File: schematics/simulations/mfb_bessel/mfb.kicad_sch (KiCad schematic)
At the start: 11 parts, among them U2 INA849D, U3 OPA182

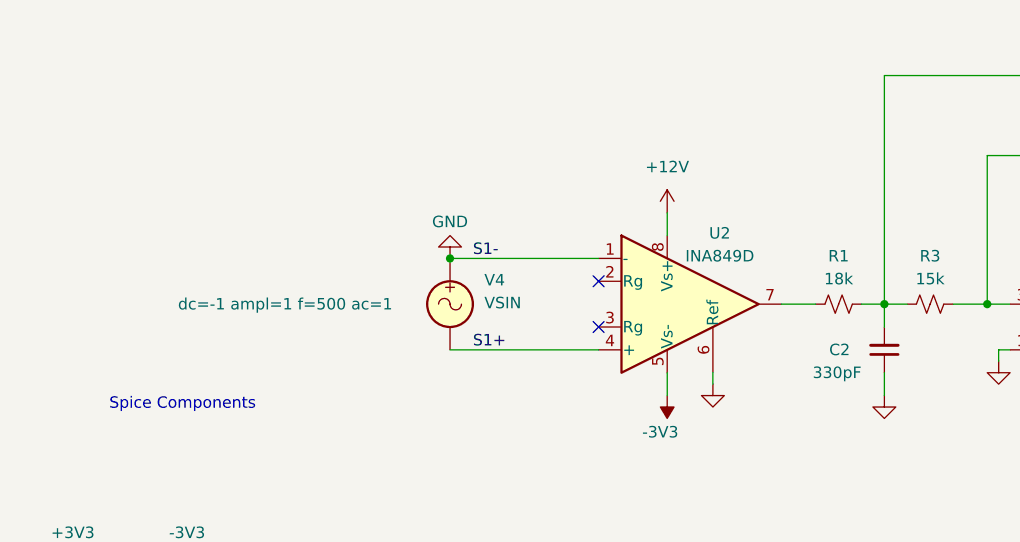
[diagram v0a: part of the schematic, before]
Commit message: feat(sim): swap for AD8422
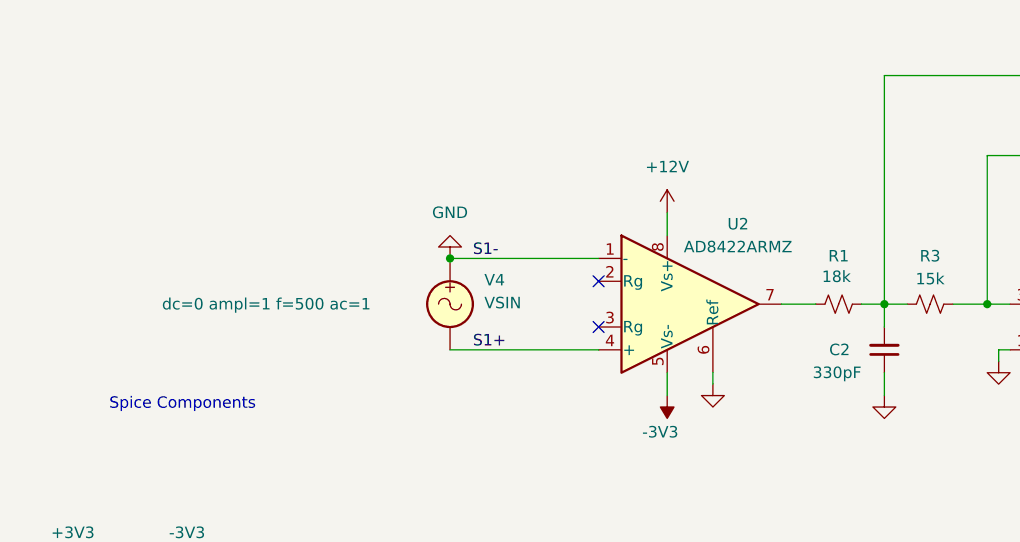
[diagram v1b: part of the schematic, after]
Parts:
- removed U2: INA849D, symbol Link-Components:INA849D
- added U2: AD8422ARMZ, symbol Amplifier_Instrumentation:AD8422ARMZ
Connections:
- net +12V: now also U2.8 (Vs+)
- net -3V3: now also U2.5 (Vs-)
- net 0: now also U2.1 (-), U2.6 (Ref)
- net S1+: now also U2.4 (+)
- net at R1.1: now also U2.7
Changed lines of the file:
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@@
+	)
+	(junction
+		(at 111.76 58.42)
+		(diameter 0)
+		(color 0 0 0 0)
 	)
 	(junction
 		(at 82.55 109.22)
-		(diameter 0)
-		(color 0 0 0 0)
-	)
-	(junction
-		(at 111.76 58.42)
 		(diameter 0)
 		(color 0 0 0 0)
@@
 			)
 		)
-		(property "Sim.Params" "dc=-1 ampl=1 f=500 ac=1"
-			(at 81.534 63.5 0)
+		(property "Sim.Params" "dc=0 ampl=1 f=500 ac=1"
+			(at 79.756 63.5 0)
 			(show_name no)
 			(do_not_autoplace no)
@@
 				(path "/404b3b71-7715-4477-a0c7-9ada934099a3"
 					(reference "R2")
-					(unit 1)
-				)
-			)
-		)
-	)
-	(symbol
-		(lib_id "power:GND")
-		(at 111.76 58.42 180)
-		(unit 1)
-		(body_style 1)
-		(exclude_from_sim no)
-		(in_bom yes)
-		(on_board yes)
-		(in_pos_files yes)
-		(dnp no)
-		(property "Reference" "#PWR019"
-			(at 111.76 52.07 0)
-			(hide yes)
-			(show_name no)
-			(do_not_autoplace no)
-			(effects
-				(font
-					(size 1.27 1.27)
-				)
-			)
-		)
-		(property "Value" "GND"
-			(at 111.76 54.356 0)
-			(show_name no)
-			(do_not_autoplace no)
-			(effects
-				(font
-					(size 1.27 1.27)
-				)
-			)
-		)
-		(property "Footprint" ""
-			(at 111.76 58.42 0)
-			(hide yes)
-			(show_name no)
-			(do_not_autoplace no)
-			(effects
-				(font
-					(size 1.27 1.27)
-				)
-			)
-		)
-		(property "Datasheet" ""
-			(at 111.76 58.42 0)
-			(hide yes)
-			(show_name no)
-			(do_not_autoplace no)
-			(effects
-				(font
-					(size 1.27 1.27)
-				)
-			)
-		)
-		(property "Description" "Power symbol creates a global label with name \"GND\" , ground"
-			(at 111.76 58.42 0)
-			(hide yes)
-			(show_name no)
-			(do_not_autoplace no)
-			(effects
-				(font
-					(size 1.27 1.27)
-				)
-			)
-		)
-		(pin "1"
-		)
-		(instances
-			(project "mfb"
-				(path "/404b3b71-7715-4477-a0c7-9ada934099a3"
-					(reference "#PWR019")
 					(unit 1)
 				)
@@
 		)
 		(property "Value" "18k"
-			(at 154.94 60.706 90)
+			(at 154.686 60.452 90)
 			(show_name no)
 			(do_not_autoplace no)
@@
 	)
 	(symbol
-		(lib_id "Link-Components:INA849D")
+		(lib_id "Amplifier_Instrumentation:AD8422ARMZ")
 		(at 135.89 63.5 0)
 		(unit 1)
@@
 		(dnp no)
 		(property "Reference" "U2"
-			(at 141.732 55.626 0)
-			(show_name no)
-			(do_not_autoplace no)
-			(effects
-				(font
-					(size 1.27 1.27)
-				)
-			)
-		)
-		(property "Value" "INA849D"
-			(at 141.732 58.166 0)
+			(at 143.764 54.61 0)
+			(show_name no)
+			(do_not_autoplace no)
+			(effects
+				(font
+					(size 1.27 1.27)
+				)
+			)
+		)
+		(property "Value" "AD8422ARMZ"
+			(at 143.764 57.15 0)
 			(show_name no)
 			(do_not_autoplace no)
@@
 		)
 		(property "Footprint" ""
-			(at 136.144 90.932 0)
-			(hide yes)
-			(show_name no)
-			(do_not_autoplace no)
-			(effects
-				(font
-					(size 1.27 1.27)
-				)
-			)
-		)
-		(property "Datasheet" "https://www.ti.com/lit/ds/symlink/ina849.pdf"
-			(at 136.398 93.472 0)
-			(hide yes)
-			(show_name no)
-			(do_not_autoplace no)
-			(effects
-				(font
-					(size 1.27 1.27)
-				)
-			)
-		)
-		(property "Description" "Ultra-Low-Noise (1 nV/√Hz), 28 MHz Bandwidth, Instrumentation Amplifier, Supply Range 8V to 36V, SOIC-8"
-			(at 135.89 88.392 0)
-			(hide yes)
-			(show_name no)
-			(do_not_autoplace no)
-			(effects
-				(font
-					(size 1.27 1.27)
-				)
-			)
-		)
-		(property "Sim.Library" "C:\\Users\\smbea\\OneDrive\\personal-files\\oats\\avena-rs\\schematics\\lib\\spice\\INA849.LIB"
+			(at 130.81 63.5 0)
+			(hide yes)
+			(show_name no)
+			(do_not_autoplace no)
+			(effects
+				(font
+					(size 1.27 1.27)
+				)
+			)
+		)
+		(property "Datasheet" "https://www.analog.com/media/en/technical-documentation/data-sheets/AD8422.pdf"
+			(at 144.78 73.66 0)
+			(hide yes)
+			(show_name no)
+			(do_not_autoplace no)
+			(effects
+				(font
+					(size 1.27 1.27)
+				)
+			)
+		)
+		(property "Description" "Low Power, Rail to Rail, Instumentation Amplifier, MSOP-8"
 			(at 135.89 63.5 0)
 			(hide yes)
@@
 			)
 		)
-		(property "Sim.Name" "INA849"
+		(property "Sim.Library" "C:\\Users\\smbea\\OneDrive\\personal-files\\oats\\avena-rs\\schematics\\lib\\spice\\AD8422.cir"
+			(at 135.89 63.5 0)
+			(hide yes)
+			(show_name no)
+			(do_not_autoplace no)
+			(effects
+				(font
+					(size 1.27 1.27)
+				)
+			)
+		)
+		(property "Sim.Name" "AD8422"
 			(at 135.89 63.5 0)
 			(hide yes)
@@
 			)
 		)
-		(property "Sim.Pins" "1=IN- 2=RG+ 3=RG- 4=IN+ 5=VEE 6=REF 7=OUT 8=VCC"
+		(property "Sim.Pins" "1=IN- 2=RG- 3=RG+ 4=IN+ 5=-Vs 6=REF 7=VOUT 8=+Vs"
 			(at 135.89 63.5 0)
 			(hide yes)
@@
 			)
 		)
+		(pin "4"
+		)
+		(pin "1"
+		)
+		(pin "2"
+		)
+		(pin "3"
+		)
 		(pin "5"
 		)
-		(pin "1"
-		)
-		(pin "3"
+		(pin "6"
+		)
+		(pin "7"
 		)
 		(pin "8"
-		)
-		(pin "7"
-		)
-		(pin "4"
-		)
-		(pin "6"
-		)
-		(pin "2"
 		)
 		(instances
@@
 					(unit 1)
 				)
+			)
+		)
+	)
+	(symbol
+		(lib_id "power:GND")
+		(at 111.76 58.42 180)
+		(unit 1)
+		(body_style 1)
+		(exclude_from_sim no)
+		(in_bom yes)
+		(on_board yes)
+		(in_pos_files yes)
+		(dnp no)
+		(fields_autoplaced yes)
+		(property "Reference" "#PWR01"
+			(at 111.76 52.07 0)
+			(hide yes)
+			(show_name no)
+			(do_not_autoplace no)
+			(effects
+				(font
+					(size 1.27 1.27)
+				)
+			)
+		)
+		(property "Value" "GND"
+			(at 111.76 53.34 0)
+			(show_name no)
+			(do_not_autoplace no)
+			(effects
+				(font
+					(size 1.27 1.27)
+				)
+			)
+		)
+		(property "Footprint" ""
+			(at 111.76 58.42 0)
+			(hide yes)
+			(show_name no)
+			(do_not_autoplace no)
+			(effects
+				(font
+					(size 1.27 1.27)
+				)
+			)
+		)
+		(property "Datasheet" ""
+			(at 111.76 58.42 0)
+			(hide yes)
+			(show_name no)
+			(do_not_autoplace no)
+			(effects
+				(font
+					(size 1.27 1.27)
+				)
+			)
+		)
+		(property "Description" "Power symbol creates a global label with name \"GND\" , ground"
+			(at 111.76 58.42 0)
+			(hide yes)
+			(show_name no)
+			(do_not_autoplace no)
+			(effects
+				(font
+					(size 1.27 1.27)
+				)
+			)
+		)
+		(pin "1"
+		)
+		(instances
+			(project "mfb"
+				(path "/404b3b71-7715-4477-a0c7-9ada934099a3"
+					(reference "#PWR01")
+					(unit 1)
+				)

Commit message: feat(signals): bessel filter
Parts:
- added C3: 220pF, Capacitor_SMD:C_0603_1608Metric, symbol Device:C_Small
- added C4: 100pF, Capacitor_SMD:C_0603_1608Metric, symbol Device:C_Small
- added R10, R8: 6.65k, Resistor_SMD:R_0603_1608Metric, symbol Device:R_Small_US
- added R4, R5, R6, R7: 100, Resistor_SMD:R_0603_1608Metric, symbol Device:R_Small_US
- added R9: 1.74k, Resistor_SMD:R_0603_1608Metric, symbol Device:R_Small_US
- added U4: AD8422ARMZ, symbol Amplifier_Instrumentation:AD8422ARMZ
- added U5: OPA182, Package_TO_SOT_SMD:SOT-353_SC-70-5, symbol Amplifier_Operational:TLV172IDCK
- added V6: VSIN, symbol Simulation_SPICE:VSIN
- C1: value 150pF -> 100pF
- C2: value 330pF -> 220pF
- R1: value 18k -> 33.2k
- R2: value 3.6k -> 6.65k
- R3: value 15k -> 1.74k
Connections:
- net +12V: now also U4.8 (Vs+)
- net +3V3: now also U5.5 (V+)
- net -3V3: now also U4.5 (Vs-), U5.2 (V-)
- net 0: now also C3.1, R4.1, R6.1, U4.6 (Ref), U5.1 (+), V6.1; no longer U2.1 (-)
- net S1+: now also R5.1; no longer U2.4 (+)
- new net: R6.2, U4.1 (-)
- new net: R7.2, U4.4 (+)
- new net: R8.1, U4.7
- new net: R5.2, U2.4 (+)
- new net: R4.2, U2.1 (-)
- new net: C3.2, R10.1, R8.2, R9.1
- new net: C4.1, R9.2, U5.3 (-)
- new net S2+: R7.1, V6.2
- new net Sc2-: C4.2, R10.2, U5.4
- no-connect marks 2 -> 4
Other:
- note added: ".meas NOISE settling_time INTEG v(onoise)"
- note added: ".options chgtol=1e-10 abstol=10u"
- moved on the sheet: V1, V3, V4, V5
